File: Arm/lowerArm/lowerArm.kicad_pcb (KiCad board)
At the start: 2 copper layers, 58.7 x 70.8 mm, 5 parts, among them J1 Screw_Terminal_01x12, J2 Screw_Terminal_01x12, U1 LM1084-5.0

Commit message: updated Arm arduino code, manual_operate, and PCBs
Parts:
- removed the REF** at (152.0, 73.1)
- added C1: 0.1uF, Capacitor_SMD:C_0805_2012Metric, F.Cu at (144.9, 128.7)
- added C2: 22pF, Capacitor_SMD:C_0805_2012Metric, F.Cu at (157.5, 119.4)
- added C3: 22pF, Capacitor_SMD:C_0805_2012Metric, F.Cu at (157.4, 114.5)
- added CAN: LED_0805_2012Metric, LED_SMD:LED_0805_2012Metric, F.Cu at (123.9, 56.5)
- added J3: Screw_Terminal_01x02, TerminalBlock_4Ucon:TerminalBlock_4Ucon_1x02_P3.50mm_Horizontal, F.Cu at (166.0, 54.9)
- added J3: Screw_Terminal_01x02, TerminalBlock_4Ucon:TerminalBlock_4Ucon_1x02_P3.50mm_Horizontal, F.Cu at (166.2, 115.9)
- added R2: 10k, Resistor_SMD:R_0805_2012Metric, F.Cu at (125.7, 124.8)
- added R3: R_US, Resistor_SMD:R_0805_2012Metric, F.Cu at (128.5, 61.1)
- added R3: R_US, Resistor_SMD:R_0805_2012Metric, F.Cu at (161.8, 127.1)
- added R3: R_US, Resistor_SMD:R_0805_2012Metric, F.Cu at (128.5, 56.5)
- added REF**: SW_SPST_EVQPE1, Button_Switch_SMD:SW_SPST_EVQPE1, F.Cu at (132.3, 131.4)
- added REF**: MountingHole_2.5mm, MountingHole:MountingHole_2.5mm, F.Cu at (172.0, 48.6)
- added REF**: PinSocket_1x02_P2.54mm_Vertical, Connector_PinSocket_2.54mm:PinSocket_1x02_P2.54mm_Vertical, F.Cu at (168.1, 127.0)
- added REF**: MountingHole_2.5mm, MountingHole:MountingHole_2.5mm, F.Cu at (171.3, 131.8)
- added REF**: MountingHole_2.5mm, MountingHole:MountingHole_2.5mm, F.Cu at (121.9, 48.3)
- added REF**: LED_0805_2012Metric, LED_SMD:LED_0805_2012Metric, F.Cu at (123.9, 61.1)
- added REF**: MountingHole_2.5mm, MountingHole:MountingHole_2.5mm, F.Cu at (121.9, 132.1)
- added U2: Crystal_Oscillator_8MHz, LFXTAL:LFXTAL057135Bulk, F.Cu at (149.9, 119.4)
- added U3: MCP2515-xSO, MCP2515_SMD:SOIC127P1030X265-18N, F.Cu at (134.5, 120.1)
- added U4: MAX3051, MAX3051:SOIC127P600X175-8N, F.Cu at (151.4, 128.6)
- moved U1 22.3 mm to (153.6, 54.5)
- moved J2 18.4 mm to (165.8, 105.2)
- moved J1 18.0 mm to (127.8, 67.1)
- moved A1 15.4 mm to (138.5, 68.2)
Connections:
- A1 pad 16: unconnected-(A1-Pad16) -> Net-(A1-Pad16)
- A1 pad 5: Net-(A1-Pad5) -> unconnected-(A1-Pad5)
- J1 pad 1: Net-(A1-Pad5) -> GND
- J1 pad 10: Net-(A1-Pad14) -> Net-(A1-Pad13)
- J1 pad 11: Net-(A1-Pad15) -> Net-(A1-Pad14)
- J1 pad 12: GND -> Net-(A1-Pad15)
- J1 pad 2: Net-(A1-Pad6) -> unconnected-(A1-Pad5)
- J1 pad 3: Net-(A1-Pad7) -> Net-(A1-Pad6)
- J1 pad 4: Net-(A1-Pad8) -> Net-(A1-Pad7)
- J1 pad 5: Net-(A1-Pad9) -> Net-(A1-Pad8)
- J1 pad 6: Net-(A1-Pad10) -> Net-(A1-Pad9)
- J1 pad 7: Net-(A1-Pad11) -> Net-(A1-Pad10)
- J1 pad 8: Net-(A1-Pad12) -> Net-(A1-Pad11)
- J1 pad 9: Net-(A1-Pad13) -> Net-(A1-Pad12)
- J2 pad 1: Net-(A1-Pad17) -> unconnected-(A1-Pad18)
- J2 pad 10: Net-(A1-Pad25) -> Net-(A1-Pad27)
- J2 pad 11: Net-(A1-Pad26) -> Net-(A1-Pad29)
- J2 pad 12: Net-(A1-Pad29) -> Net-(A1-Pad30)
- J2 pad 2: Net-(A1-Pad27) -> Net-(A1-Pad19)
- J2 pad 3: Net-(A1-Pad28) -> Net-(A1-Pad20)
- J2 pad 4: Net-(A1-Pad19) -> Net-(A1-Pad21)
- J2 pad 5: Net-(A1-Pad20) -> Net-(A1-Pad22)
- J2 pad 6: Net-(A1-Pad21) -> Net-(A1-Pad23)
- J2 pad 7: Net-(A1-Pad22) -> Net-(A1-Pad24)
- J2 pad 8: Net-(A1-Pad23) -> Net-(A1-Pad25)
- J2 pad 9: Net-(A1-Pad24) -> Net-(A1-Pad26)
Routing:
- net Net-(A1-Pad17): track 18.3 -> 78.9 mm, vias 0 -> 2
- net Net-(A1-Pad26): track 13.7 -> 58.8 mm, vias 0 -> 1
- net Net-(A1-Pad16): track 0.00 -> 44.7 mm
- net GND: track 107.3 -> 64.2 mm, vias 0 -> 8
- net Net-(A1-Pad25): track 13.4 -> 56.3 mm, vias 0 -> 1
- net Net-(A1-Pad28): track 39.0 -> 0.85 mm
- net Net-(A1-Pad13): track 13.2 -> 43.8 mm
- net Net-(A1-Pad27): track 40.0 -> 12.9 mm
- net Net-(J3-Pad2): track 0.00 -> 25.8 mm
- net Net-(J3-Pad1): track 0.00 -> 23.7 mm
- net Net-(A1-Pad14): track 12.8 -> 35.5 mm, vias 0 -> 1
- net Net-(A1-Pad15): track 12.7 -> 34.9 mm
- net Net-(C2-Pad1): track 0.00 -> 19.1 mm
- net unconnected-(A1-Pad5): track 0.00 -> 18.5 mm
- net unconnected-(A1-Pad18): track 0.00 -> 18.4 mm
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- added copper zone on B.Cu, net GND
- added copper zone on F.Cu, net Net-(A1-Pad30)
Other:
- board size 58.7 x 70.8 mm -> 57.3 x 91.3 mm
- board text added: "GND"
- board text added: "GND D2 D3 D4 D5 D6 D7 D8 D9 D10 D11 D12"
- board text added: "H"
- board text added: "Jack Cornette"
- board text added: "L"
- board text added: "Spring 2023 Capstone"
- board text added: "VCC"
- board text added: "VIN GND 5V A7 A6 A5 A4 A3 A2 A1 A0 REF"

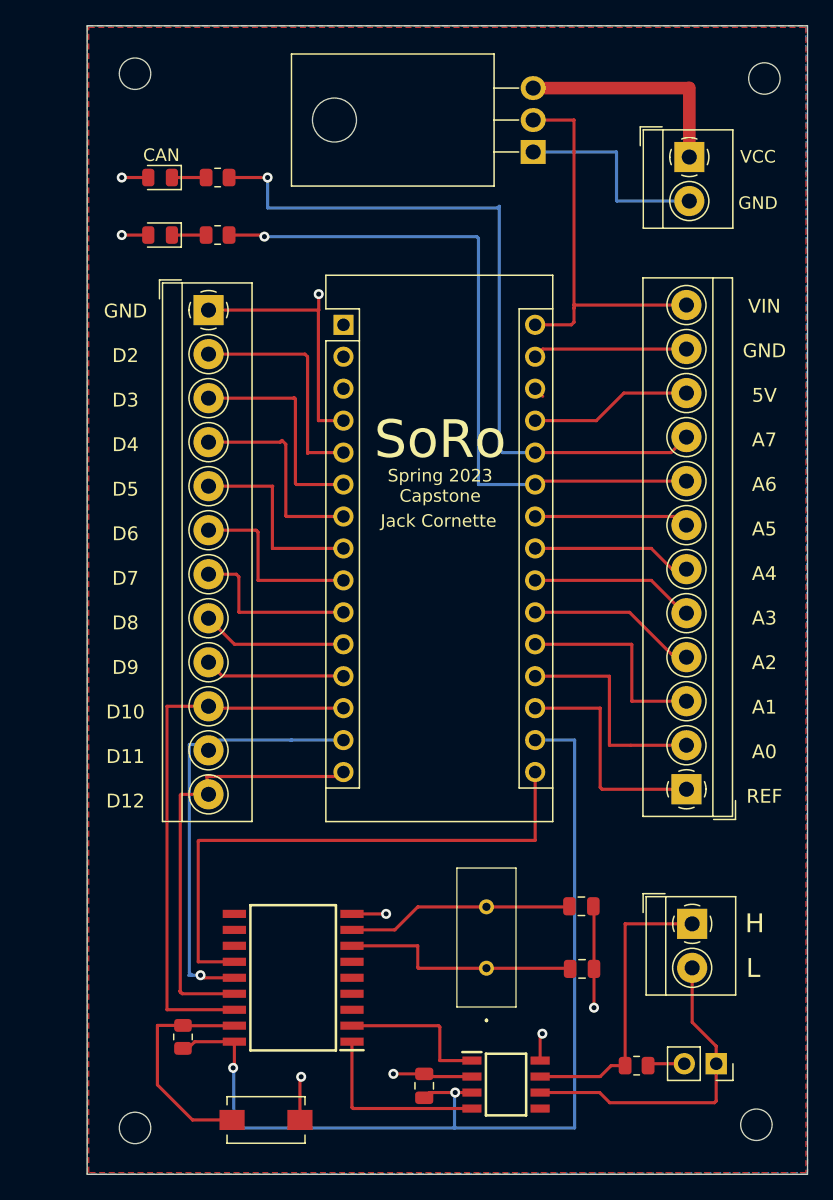
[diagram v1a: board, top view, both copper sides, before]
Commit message: Updated wheel code, organized, added a folder for examples I'vemade
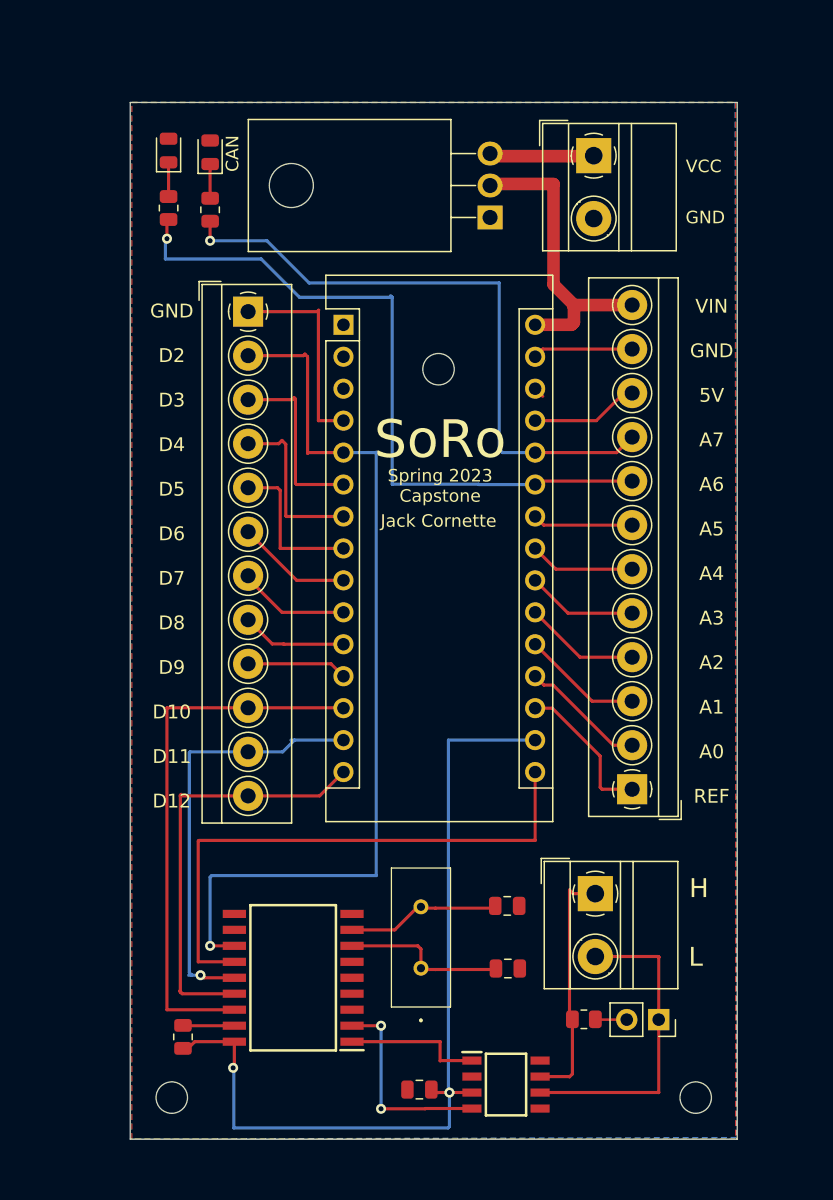
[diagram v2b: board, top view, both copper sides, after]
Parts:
- removed the REF** at (132.3, 131.4)
- removed the REF** at (172.0, 48.6)
- J3 (x2): footprint TerminalBlock_4Ucon:TerminalBlock_4Ucon_1x02_P3.50mm_Horizontal -> TerminalBlock_MetzConnect:TerminalBlock_MetzConnect_Type011_RT05502HBWC_1x02_P5.00mm_Horizontal
- moved REF** 33.7 mm to (146.1, 71.8)
- moved J3 8.07 mm to (158.5, 113.5)
- moved J3 7.60 mm to (158.4, 54.8)
- moved REF** 6.75 mm to (124.6, 54.4), turned to 90 degrees
- moved U1 6.23 mm to (150.1, 59.7)
- moved C2 5.90 mm to (151.6, 119.4)
- moved C3 5.90 mm to (151.5, 114.4)
- moved REF** 5.76 mm to (163.6, 123.5)
- moved R3 5.58 mm to (157.6, 123.4)
- moved REF** 5.29 mm to (166.5, 129.7)
- moved U2 5.21 mm to (144.7, 119.4)
- moved CAN 4.45 mm to (127.9, 54.5), turned to 90 degrees
- moved R3 4.45 mm to (124.6, 58.9), turned to -90 degrees
- moved J2 4.32 mm to (161.4, 105.2)
- moved REF** 3.79 mm to (124.8, 129.7)
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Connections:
- A1 pad 5: unconnected-(A1-Pad5) -> unconnected-(U3-Pad12)
- J1 pad 2: unconnected-(A1-Pad5) -> unconnected-(U3-Pad12)
- U4 pad 1: Net-(U3-Pad2) -> Net-(U3-Pad1)
- U4 pad 4: Net-(U3-Pad1) -> Net-(U3-Pad2)
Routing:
- net unconnected-(U3-Pad12): track 0.00 -> 72.3 mm, vias 0 -> 1
- net GND: track 64.2 -> 16.5 mm, vias 8 -> 0
- net unconnected-(A1-Pad5): track 18.5 -> 0.00 mm
- net Net-(R2-Pad1): track 17.7 -> 3.85 mm
- net Net-(A1-Pad17): track 78.9 -> 68.6 mm
- net Net-(A1-Pad26): track 58.8 -> 50.4 mm
- net Net-(A1-Pad19): track 18.2 -> 10.5 mm
- net Net-(A1-Pad20): track 16.5 -> 9.59 mm
- net Net-(A1-Pad30): track 31.4 -> 24.5 mm
- net unconnected-(A1-Pad18): track 18.4 -> 11.8 mm
- net Net-(C3-Pad1): track 18.1 -> 12.2 mm
- net Net-(C2-Pad1): track 19.1 -> 13.5 mm
- net Net-(A1-Pad9): track 14.6 -> 9.40 mm
- net +BATT: track 18.0 -> 12.8 mm
- net Net-(A1-Pad27): track 12.9 -> 7.97 mm
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- added copper zone on F.Cu, net GND
- removed copper zone on F.Cu, net Net-(A1-Pad30)
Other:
- board size 57.3 x 91.3 mm -> 48.3 x 82.4 mm
